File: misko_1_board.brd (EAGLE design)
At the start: 115 x 115 mm, 150 parts, among them IC1 ATMEGA1281-16AU, IC10 ORG1510-MK4, IC11 TPS3808G33DBVT, IC12 LTC4425, IC13 RN4678_BT_MODULE, IC14 ADXL345, IC15 74HCT1G32, IC16 FM25W256-SOIC, IC17 MICROSD_SPI_MODE, IC18 FH12-30S-0.5SH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

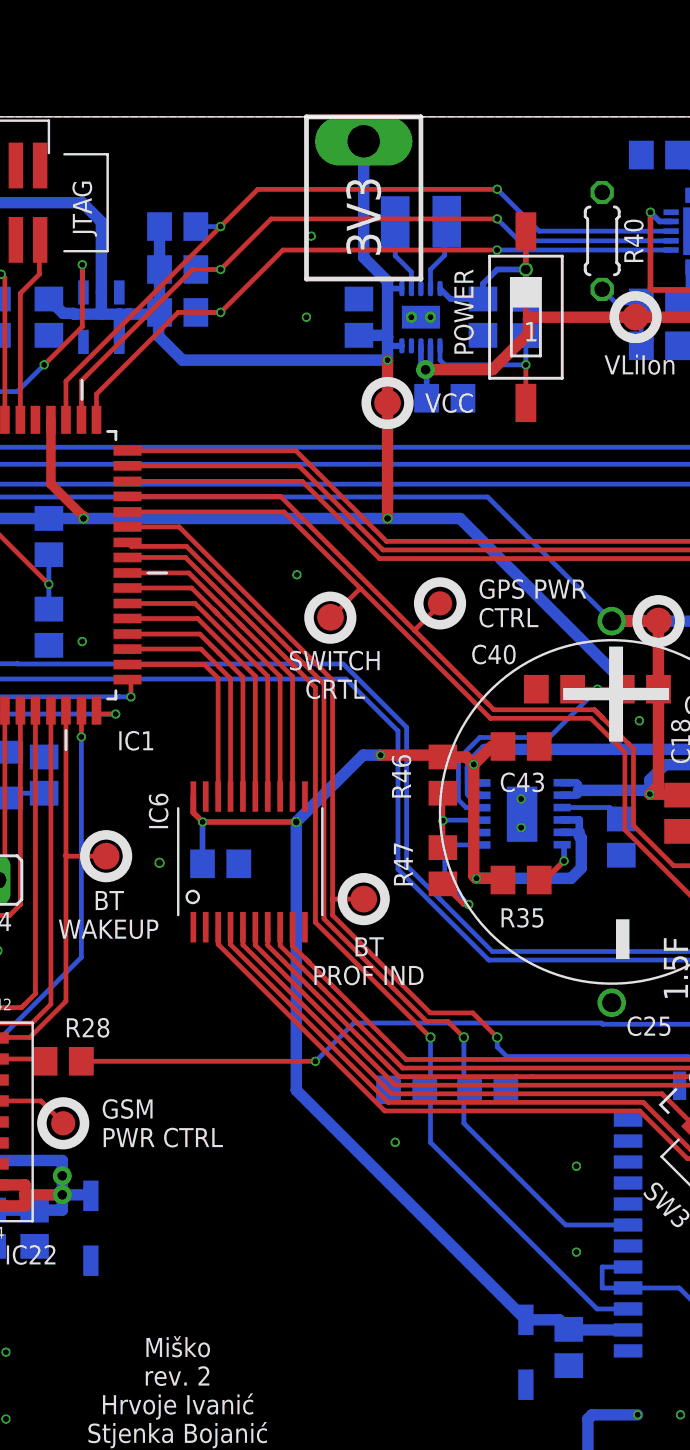
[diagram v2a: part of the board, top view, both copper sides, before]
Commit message: - added 3V3 zener protection diode
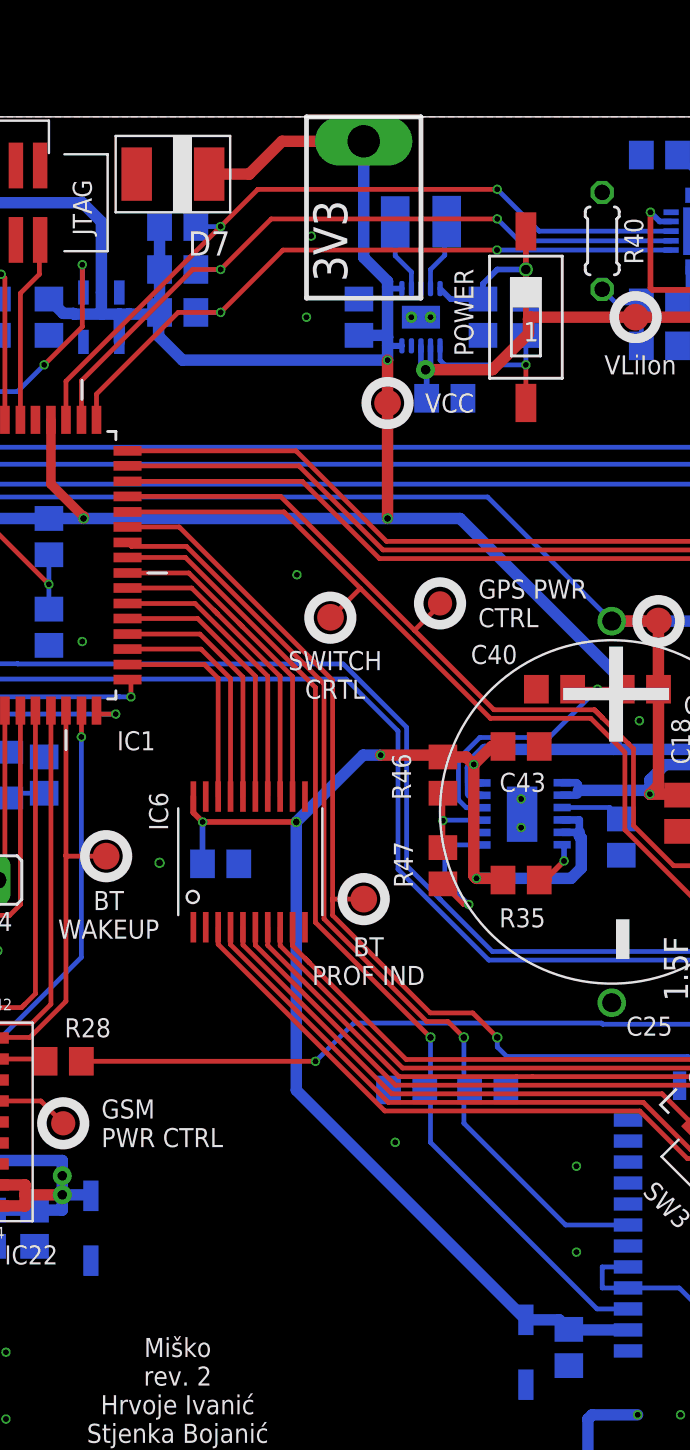
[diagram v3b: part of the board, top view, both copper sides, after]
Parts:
- added D7: (no value), zener:DO-214
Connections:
- net 5V0: now also D6.CAT; no longer D6.C
- net GND: now also D3.AN, D4.AN, D5.AN, D6.AN, D7.AN; no longer D3.A, D4.A, D5.A, D6.A
- net VCC: now also D4.CAT, D7.CAT; no longer D4.C
- net V_LIION+: now also D3.CAT, D5.CAT; no longer D3.C, D5.C
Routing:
- net VCC: track 508.6 -> 517.4 mm
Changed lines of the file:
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@@
 <text x="86.605" y="46.565" size="1" layer="21" font="vector" align="center">VGPS</text>
 <text x="72" y="58" size="1" layer="21" font="vector" align="center">VCC</text>
-<text x="67.5" y="67.75" size="1.778" layer="21" font="vector" rot="R90" align="center">3V3</text>
+<text x="65.75" y="66.5" size="1.778" layer="21" font="vector" rot="R90" align="center">3V3</text>
 <text x="104" y="67.25" size="1.778" layer="21" font="vector" rot="R90" align="center">VUSB</text>
 <text x="113.5" y="69.5" size="1" layer="21" font="vector" align="center">GND</text>
@@
 <text x="12.25" y="28.25" size="1" layer="21" font="vector" align="center">WiFi RST</text>
 <wire x1="64.5" y1="73" x2="70.5" y2="73" width="0.25" layer="21"/>
-<wire x1="70.5" y1="73" x2="70.5" y2="64.5" width="0.25" layer="21"/>
-<wire x1="70.5" y1="64.5" x2="64.5" y2="64.5" width="0.25" layer="21"/>
-<wire x1="64.5" y1="64.5" x2="64.5" y2="73" width="0.25" layer="21"/>
+<wire x1="70.5" y1="73" x2="70.5" y2="63.5" width="0.25" layer="21"/>
+<wire x1="70.5" y1="63.5" x2="64.5" y2="63.5" width="0.25" layer="21"/>
+<wire x1="64.5" y1="63.5" x2="64.5" y2="73" width="0.25" layer="21"/>
 <wire x1="95.75" y1="73" x2="101" y2="73" width="0.25" layer="21"/>
 <wire x1="101" y1="73" x2="101" y2="63.5" width="0.25" layer="21"/>
@@
 <attribute name="VALUE" x="96.875" y="69.57" size="1.016" layer="27" ratio="18" rot="R270"/>
 </element>
+<element name="D7" library="zener" library_urn="urn:adsk.eagle:library:449000" package="DO-214" value="" x="57.5" y="70" rot="R180"/>
 </elements>
 <signals>
@@
 <wire x1="41.25" y1="68.5" x2="52.75" y2="68.5" width="0.6" layer="16"/>
 <wire x1="52.75" y1="68.5" x2="53.75" y2="67.5" width="0.6" layer="16"/>
-<contactref element="D4" pad="C"/>
+<contactref element="D4" pad="CAT"/>
 <wire x1="76" y1="9.95" x2="77.75" y2="9.95" width="0.6" layer="16"/>
-<wire x1="77.75" y1="9.95" x2="78.28" y2="9.42" width="0.6" layer="16"/>
+<wire x1="77.75" y1="9.95" x2="78.25" y2="9.45" width="0.6" layer="16"/>
 <wire x1="63.965665625" y1="21.984334375" x2="76" y2="9.95" width="0.6" layer="16"/>
 <wire x1="63.965665625" y1="36.04305625" x2="63.965665625" y2="21.984334375" width="0.6" layer="16"/>
+<contactref element="D7" pad="CAT"/>
+<wire x1="67.5" y1="71.72" x2="63.22" y2="71.72" width="0.6" layer="1"/>
+<wire x1="63.22" y1="71.72" x2="61.5" y2="70" width="0.6" layer="1"/>
+<wire x1="61.5" y1="70" x2="59.4" y2="70" width="0.6" layer="1"/>
 </signal>
 <signal name="GND">
@@
 <via x="65" y="1.25" extent="1-16" drill="0.3"/>
 <contactref element="C26" pad="1"/>
-<contactref element="D3" pad="A"/>
+<contactref element="D3" pad="AN"/>
 <via x="31.9" y="33.8" extent="1-16" drill="0.35"/>
 <via x="56.8" y="33.9" extent="1-16" drill="0.35"/>
@@
 <contactref element="IC6" pad="!EN!"/>
 <contactref element="C45" pad="2"/>
-<contactref element="D5" pad="A"/>
-<contactref element="D4" pad="A"/>
-<contactref element="D6" pad="A"/>
+<contactref element="D5" pad="AN"/>
+<contactref element="D4" pad="AN"/>
+<contactref element="D6" pad="AN"/>
+<contactref element="D7" pad="AN"/>
 <wire x1="85.5" y1="67" x2="85.49" y2="67.01" width="0" layer="19" extent="16-16"/>
 <wire x1="32.25" y1="41" x2="31.5" y2="44.5" width="0" layer="19" extent="1-1"/>
@@
 <wire x1="89.25" y1="66.95" x2="89.25" y2="67.029665625" width="0.6" layer="16"/>
 <wire x1="89.25" y1="67.029665625" x2="89.229665625" y2="67.05" width="0.6" layer="16"/>
-<contactref element="D6" pad="C"/>
+<contactref element="D6" pad="CAT"/>
 <wire x1="99.415" y1="68.73" x2="99.415" y2="71.185" width="0.6" layer="1"/>
 <wire x1="99.415" y1="71.185" x2="99.4" y2="71.2" width="0.6" layer="1"/>
@@
 <wire x1="92.25" y1="67.2" x2="92.3" y2="67.2" width="0.6" layer="1"/>
 <contactref element="C26" pad="2"/>
-<contactref element="D3" pad="C"/>
+<contactref element="D3" pad="CAT"/>
 <wire x1="48" y1="15.7" x2="50.25" y2="15.7" width="0.6" layer="16"/>
 <wire x1="51.7" y1="18.3" x2="44.25" y2="18.3" width="0.6" layer="16"/>
@@
 <wire x1="93.5" y1="67.25" x2="92.3" y2="67.25" width="0.6" layer="1"/>
 <wire x1="92.3" y1="67.25" x2="92.25" y2="67.2" width="0.6" layer="1"/>
-<contactref element="D5" pad="C"/>
+<contactref element="D5" pad="CAT"/>
 <wire x1="24.13" y1="38.95" x2="24.13" y2="41.33" width="0.6" layer="1"/>
 <wire x1="24.13" y1="41.33" x2="24.11" y2="41.35" width="0.6" layer="1"/>

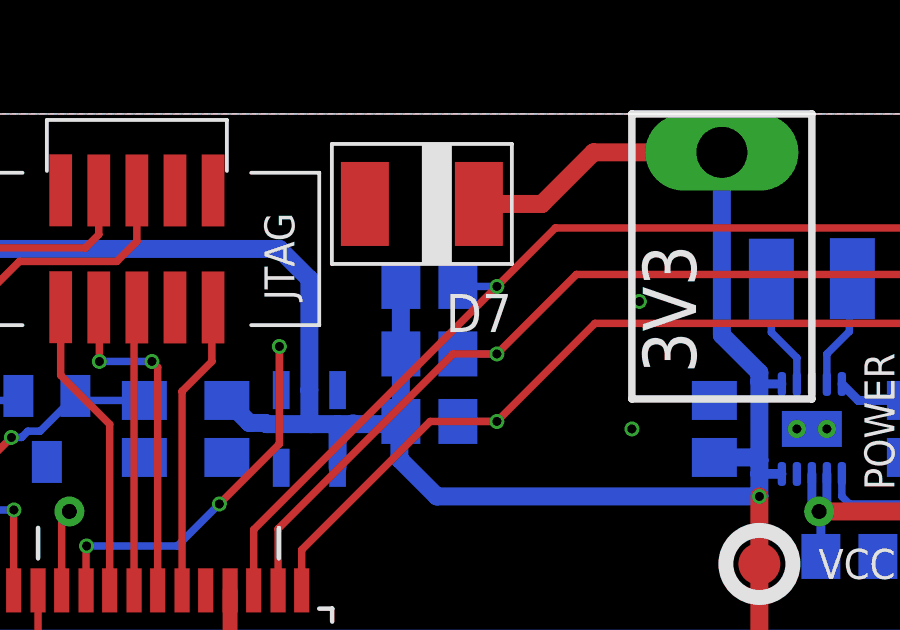
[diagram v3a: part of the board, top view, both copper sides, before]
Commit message: - specified value for 3V3 protection diode (is in reality a 3V8 diode)
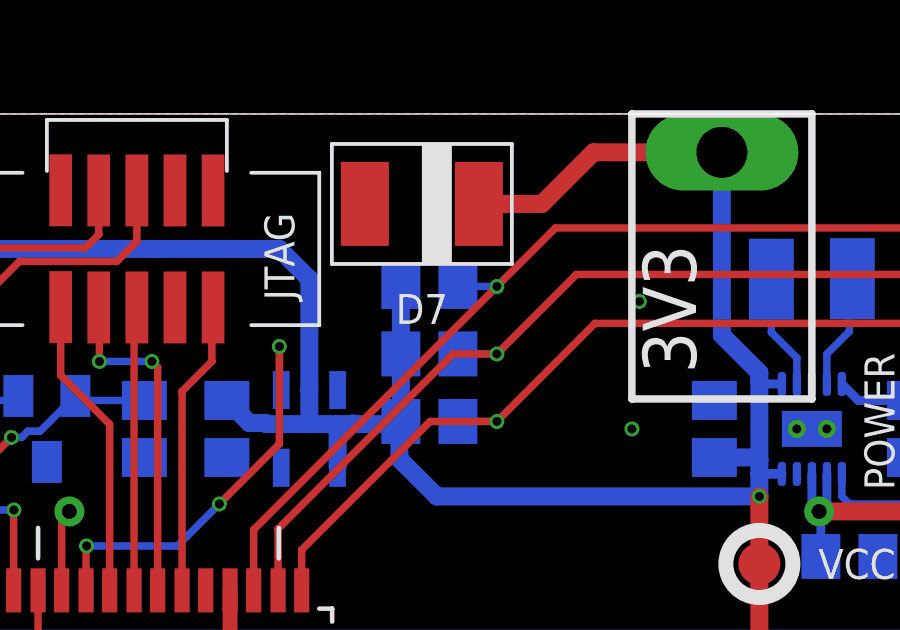
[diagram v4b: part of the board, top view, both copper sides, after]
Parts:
- D7: value (none) -> BZG05C3V6-E3-TR3
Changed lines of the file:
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@@
 <layer number="20" name="Dimension" color="15" fill="1" visible="yes" active="yes"/>
 <layer number="21" name="tPlace" color="7" fill="1" visible="yes" active="yes"/>
-<layer number="22" name="bPlace" color="7" fill="1" visible="no" active="yes"/>
+<layer number="22" name="bPlace" color="7" fill="1" visible="yes" active="yes"/>
 <layer number="23" name="tOrigins" color="15" fill="1" visible="yes" active="yes"/>
-<layer number="24" name="bOrigins" color="15" fill="1" visible="no" active="yes"/>
+<layer number="24" name="bOrigins" color="15" fill="1" visible="yes" active="yes"/>
 <layer number="25" name="tNames" color="7" fill="1" visible="yes" active="yes"/>
-<layer number="26" name="bNames" color="7" fill="1" visible="no" active="yes"/>
+<layer number="26" name="bNames" color="7" fill="1" visible="yes" active="yes"/>
 <layer number="27" name="tValues" color="7" fill="1" visible="no" active="yes"/>
 <layer number="28" name="bValues" color="7" fill="1" visible="no" active="yes"/>
@@
 <layer number="38" name="bTest" color="7" fill="1" visible="no" active="yes"/>
 <layer number="39" name="tKeepout" color="4" fill="11" visible="yes" active="yes"/>
-<layer number="40" name="bKeepout" color="1" fill="11" visible="no" active="yes"/>
+<layer number="40" name="bKeepout" color="1" fill="11" visible="yes" active="yes"/>
 <layer number="41" name="tRestrict" color="4" fill="10" visible="yes" active="yes"/>
-<layer number="42" name="bRestrict" color="1" fill="10" visible="no" active="yes"/>
+<layer number="42" name="bRestrict" color="1" fill="10" visible="yes" active="yes"/>
 <layer number="43" name="vRestrict" color="2" fill="10" visible="no" active="yes"/>
 <layer number="44" name="Drills" color="7" fill="1" visible="yes" active="yes"/>
 <layer number="45" name="Holes" color="7" fill="1" visible="yes" active="yes"/>
 <layer number="46" name="Milling" color="3" fill="1" visible="yes" active="yes"/>
-<layer number="47" name="Measures" color="7" fill="1" visible="yes" active="yes"/>
+<layer number="47" name="Measures" color="7" fill="1" visible="no" active="yes"/>
 <layer number="48" name="Document" color="7" fill="1" visible="yes" active="yes"/>
 <layer number="49" name="Reference" color="7" fill="1" visible="no" active="yes"/>
 <layer number="50" name="dxf" color="7" fill="1" visible="no" active="no"/>
 <layer number="51" name="tDocu" color="7" fill="1" visible="yes" active="yes"/>
-<layer number="52" name="bDocu" color="7" fill="1" visible="no" active="yes"/>
+<layer number="52" name="bDocu" color="7" fill="1" visible="yes" active="yes"/>
 <layer number="53" name="tGND_GNDA" color="7" fill="9" visible="no" active="no"/>
 <layer number="54" name="bGND_GNDA" color="1" fill="9" visible="no" active="no"/>
@@
 <attribute name="VALUE" x="96.875" y="69.57" size="1.016" layer="27" ratio="18" rot="R270"/>
 </element>
-<element name="D7" library="zener" library_urn="urn:adsk.eagle:library:449000" package="DO-214" value="" x="57.5" y="70" rot="R180"/>
+<element name="D7" library="zener" library_urn="urn:adsk.eagle:library:449000" package="DO-214" value="BZG05C3V6-E3-TR3" x="57.5" y="70" smashed="yes" rot="R180">
+<attribute name="NAME" x="57.5" y="66.5" size="1" layer="21" font="vector" rot="R180" align="center"/>
+</element>
 </elements>
 <signals>

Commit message: - corrected values for oscillator load capacitors
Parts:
- C12, C8: value 15pF -> 7pF
- Q1: value ABM3B -> ABM3B-8MHZ-10-1-U-T
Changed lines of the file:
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@@
 <layer number="14" name="Route14" color="1" fill="6" visible="no" active="no"/>
 <layer number="15" name="Route15" color="4" fill="6" visible="no" active="no"/>
-<layer number="16" name="Bottom" color="1" fill="1" visible="yes" active="yes"/>
+<layer number="16" name="Bottom" color="1" fill="1" visible="no" active="yes"/>
 <layer number="17" name="Pads" color="2" fill="1" visible="yes" active="yes"/>
 <layer number="18" name="Vias" color="2" fill="1" visible="yes" active="yes"/>
@@
 <layer number="20" name="Dimension" color="15" fill="1" visible="yes" active="yes"/>
 <layer number="21" name="tPlace" color="7" fill="1" visible="yes" active="yes"/>
-<layer number="22" name="bPlace" color="7" fill="1" visible="yes" active="yes"/>
+<layer number="22" name="bPlace" color="7" fill="1" visible="no" active="yes"/>
 <layer number="23" name="tOrigins" color="15" fill="1" visible="yes" active="yes"/>
-<layer number="24" name="bOrigins" color="15" fill="1" visible="yes" active="yes"/>
+<layer number="24" name="bOrigins" color="15" fill="1" visible="no" active="yes"/>
 <layer number="25" name="tNames" color="7" fill="1" visible="yes" active="yes"/>
-<layer number="26" name="bNames" color="7" fill="1" visible="yes" active="yes"/>
+<layer number="26" name="bNames" color="7" fill="1" visible="no" active="yes"/>
 <layer number="27" name="tValues" color="7" fill="1" visible="no" active="yes"/>
 <layer number="28" name="bValues" color="7" fill="1" visible="no" active="yes"/>
@@
 <layer number="38" name="bTest" color="7" fill="1" visible="no" active="yes"/>
 <layer number="39" name="tKeepout" color="4" fill="11" visible="yes" active="yes"/>
-<layer number="40" name="bKeepout" color="1" fill="11" visible="yes" active="yes"/>
+<layer number="40" name="bKeepout" color="1" fill="11" visible="no" active="yes"/>
 <layer number="41" name="tRestrict" color="4" fill="10" visible="yes" active="yes"/>
-<layer number="42" name="bRestrict" color="1" fill="10" visible="yes" active="yes"/>
+<layer number="42" name="bRestrict" color="1" fill="10" visible="no" active="yes"/>
 <layer number="43" name="vRestrict" color="2" fill="10" visible="no" active="yes"/>
 <layer number="44" name="Drills" color="7" fill="1" visible="yes" active="yes"/>
 <layer number="45" name="Holes" color="7" fill="1" visible="yes" active="yes"/>
 <layer number="46" name="Milling" color="3" fill="1" visible="yes" active="yes"/>
-<layer number="47" name="Measures" color="7" fill="1" visible="no" active="yes"/>
+<layer number="47" name="Measures" color="7" fill="1" visible="yes" active="yes"/>
 <layer number="48" name="Document" color="7" fill="1" visible="yes" active="yes"/>
 <layer number="49" name="Reference" color="7" fill="1" visible="no" active="yes"/>
 <layer number="50" name="dxf" color="7" fill="1" visible="no" active="no"/>
 <layer number="51" name="tDocu" color="7" fill="1" visible="yes" active="yes"/>
-<layer number="52" name="bDocu" color="7" fill="1" visible="yes" active="yes"/>
+<layer number="52" name="bDocu" color="7" fill="1" visible="no" active="yes"/>
 <layer number="53" name="tGND_GNDA" color="7" fill="9" visible="no" active="no"/>
 <layer number="54" name="bGND_GNDA" color="1" fill="9" visible="no" active="no"/>
@@
 <attribute name="VALUE" x="25.23" y="6.29" size="1.27" layer="28" rot="MR180"/>
 </element>
-<element name="C8" library="resistor" library_urn="urn:adsk.eagle:library:348" package="C0805" value="15pF" x="42.75" y="38.5" smashed="yes" rot="MR90">
+<element name="C8" library="resistor" library_urn="urn:adsk.eagle:library:348" package="C0805" value="7pF" x="42.75" y="38.5" smashed="yes" rot="MR90">
 <attribute name="NAME" x="41.235" y="38.495" size="1" layer="26" font="vector" rot="MR270" align="center"/>
 <attribute name="VALUE" x="40.21" y="37.23" size="1.27" layer="28" rot="MR90"/>
 </element>
-<element name="C12" library="resistor" library_urn="urn:adsk.eagle:library:348" package="C0805" value="15pF" x="50.75" y="38.5" smashed="yes" rot="MR270">
+<element name="C12" library="resistor" library_urn="urn:adsk.eagle:library:348" package="C0805" value="7pF" x="50.75" y="38.5" smashed="yes" rot="MR270">
 <attribute name="NAME" x="50.905" y="34.74" size="1" layer="26" font="vector" rot="MR90" align="center"/>
 <attribute name="VALUE" x="53.29" y="39.77" size="1.27" layer="28" rot="MR270"/>
@@
 <attribute name="VALUE" x="32.182" y="10.6834" size="1.27" layer="27" rot="R180"/>
 </element>
-<element name="Q1" library="ABM3B-8MHZ-10-1-U-T - Quartz Resonator" package="SMT" value="ABM3B" x="46.75" y="38.5" smashed="yes" rot="MR180">
+<element name="Q1" library="ABM3B-8MHZ-10-1-U-T - Quartz Resonator" package="SMT" value="ABM3B-8MHZ-10-1-U-T" x="46.75" y="38.5" smashed="yes" rot="MR180">
 <attribute name="NAME" x="46.73" y="35.63" size="1" layer="26" font="vector" rot="MR180" align="center"/>
 <attribute name="VALUE" x="43.75" y="42.5" size="1.27" layer="28" rot="MR180"/>
